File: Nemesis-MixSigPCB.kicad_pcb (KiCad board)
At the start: 4 copper layers, 50 x 60 mm, 113 parts, among them J200 USB_C_Receptacle_USB2.0, J201 2x5 1.27mm, J300 031-5640-1010, J400 031-5640-1010, U100 HT7533-1, U101 TLV62569DBV, U102 MCP6001T-E/OT, U200 STM32F103CBT6, U201 USBLC6-2SC6, U300 MCP6001T-E/OT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

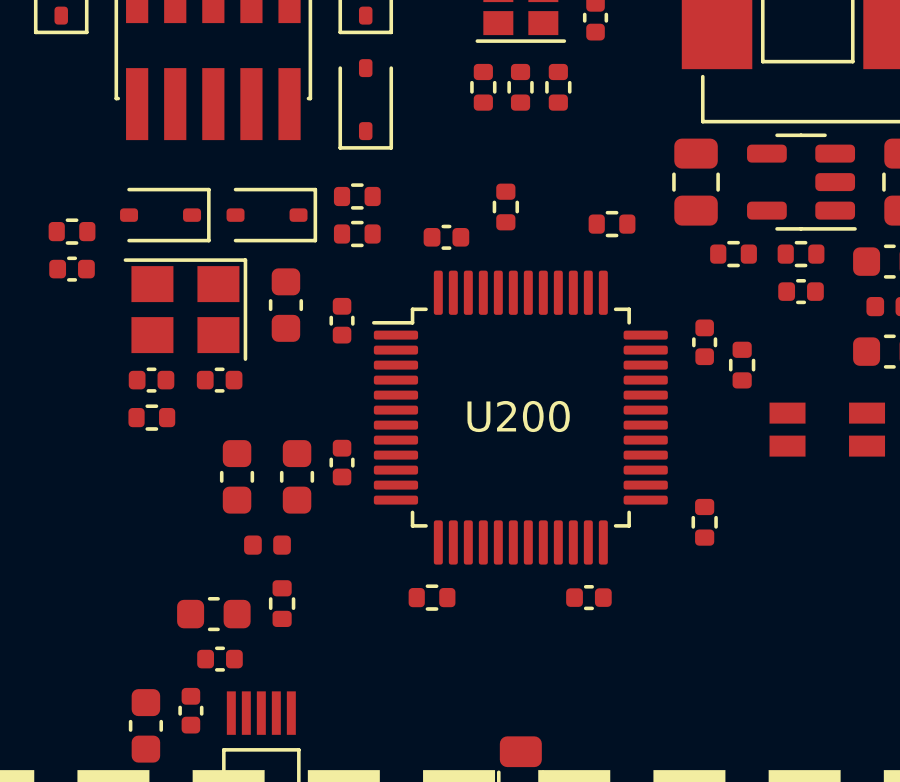
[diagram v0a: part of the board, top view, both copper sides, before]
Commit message: Routed uController Basic Tracks
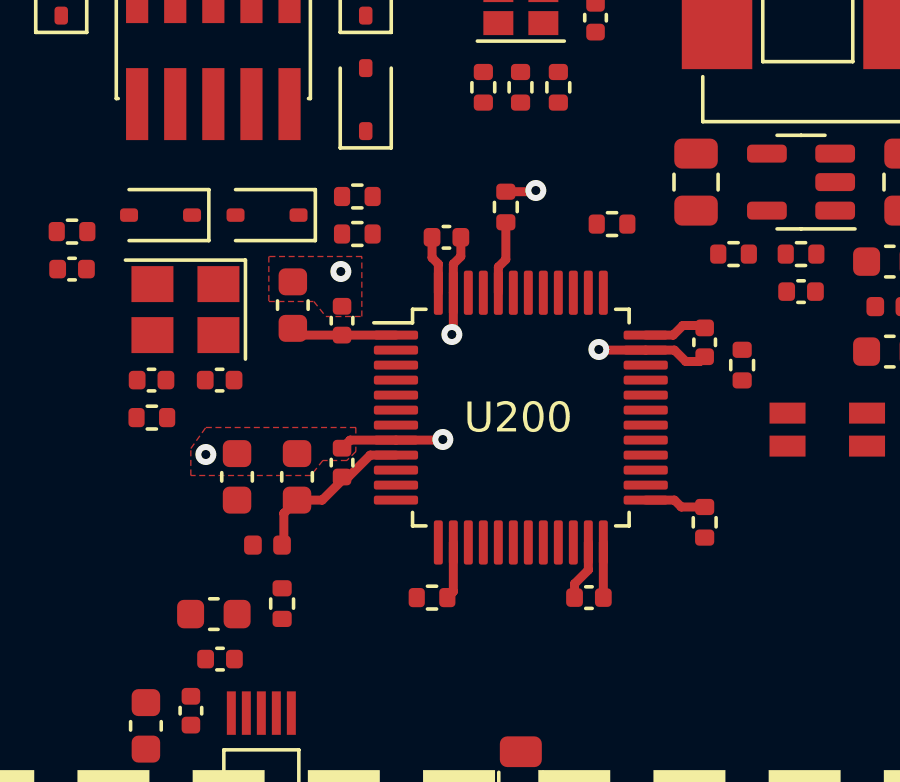
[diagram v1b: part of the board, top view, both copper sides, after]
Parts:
- moved C200 0.23 mm to (137.4, 79.2)
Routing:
- net GND: track 0.00 -> 13.6 mm, vias 0 -> 6
- net +3V3: track 0.00 -> 9.43 mm
- net VDDA: track 0.00 -> 5.69 mm
- net /MCU/BOOT0: track 0.00 -> 2.45 mm
- net SPI2_NSS: track 0.00 -> 2.06 mm
- net SPI1_NSS: track 0.00 -> 1.92 mm
- added copper zone on F.Cu, net GND
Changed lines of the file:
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@@
   )
   (footprint "Capacitor_SMD:C_0603_1608Metric" (layer "F.Cu")
-    (at 137.17 79.22 90)
+    (at 137.4 79.22 90)
     (descr "Capacitor SMD 0603 (1608 Metric), square (rectangular) end terminal, IPC_7351 nominal, (Body size source: IPC-SM-782 page 76, https://www.pcb-3d.com/wordpress/wp-content/uploads/ipc-sm-782a_amendment_1_and_2.pdf), generated with kicad-footprint-generator")
     (tags "capacitor")
@@
     (style (thickness 0.1) (arrow_length 1.27) (text_position_mode 0) (extension_height 0.58642) (extension_offset 0.5) keep_text_aligned)
   )
+  (segment (start 147.25 88.05) (end 146.79 88.51) (width 0.3) (layer "F.Cu") (net 2))
+  (segment (start 140.8375 83.72) (end 142.38 83.72) (width 0.3) (layer "F.Cu") (net 2))
+  (segment (start 149.1625 80.72) (end 150.12 80.72) (width 0.3) (layer "F.Cu") (net 2))
+  (segment (start 143 77.6) (end 143 76.96) (width 0.3) (layer "F.Cu") (net 2))
+  (segment (start 142.38 83.72) (end 142.4 83.7) (width 0.3) (layer "F.Cu") (net 2))
+  (segment (start 142.75 78.8075) (end 142.75 80.15) (width 0.3) (layer "F.Cu") (net 2))
+  (segment (start 145.46 75.44) (end 145.5 75.4) (width 0.3) (layer "F.Cu") (net 2))
+  (segment (start 142.75 78.8075) (end 142.75 77.85) (width 0.3) (layer "F.Cu") (net 2))
+  (segment (start 147.25 87.1325) (end 147.25 88.05) (width 0.3) (layer "F.Cu") (net 2))
+  (segment (start 144.5 75.44) (end 145.46 75.44) (width 0.3) (layer "F.Cu") (net 2))
+  (segment (start 142.75 80.15) (end 142.7 80.2) (width 0.3) (layer "F.Cu") (net 2))
+  (segment (start 146.79 88.51) (end 146.79 88.97) (width 0.3) (layer "F.Cu") (net 2))
+  (segment (start 150.5 81.1) (end 150.9675 81.1) (width 0.3) (layer "F.Cu") (net 2))
+  (segment (start 139.31 83.72) (end 139.04 83.99) (width 0.3) (layer "F.Cu") (net 2))
+  (segment (start 142.75 77.85) (end 143 77.6) (width 0.3) (layer "F.Cu") (net 2))
+  (segment (start 150.12 80.72) (end 150.5 81.1) (width 0.3) (layer "F.Cu") (net 2))
+  (segment (start 147.62 80.72) (end 147.6 80.7) (width 0.3) (layer "F.Cu") (net 2))
+  (segment (start 149.1625 80.72) (end 147.62 80.72) (width 0.3) (layer "F.Cu") (net 2))
+  (segment (start 150.9675 81.1) (end 151.1275 80.94) (width 0.3) (layer "F.Cu") (net 2))
+  (segment (start 140.8375 83.72) (end 139.31 83.72) (width 0.3) (layer "F.Cu") (net 2))
+  (via (at 142.4 83.7) (size 0.7) (drill 0.3) (layers "F.Cu" "B.Cu") (net 2))
+  (via (at 142.7 80.2) (size 0.7) (drill 0.3) (layers "F.Cu" "B.Cu") (net 2))
+  (via (at 147.6 80.7) (size 0.7) (drill 0.3) (layers "F.Cu" "B.Cu") (net 2))
+  (via (at 145.5 75.4) (size 0.7) (drill 0.3) (layers "F.Cu" "B.Cu") (net 2))
+  (via (at 139 78.1) (size 0.7) (drill 0.3) (layers "F.Cu" "B.Cu") (free) (net 2))
+  (via (at 134.5 84.2) (size 0.7) (drill 0.3) (layers "F.Cu" "B.Cu") (free) (net 2))
+  (segment (start 142.25 77.85) (end 142.04 77.64) (width 0.3) (layer "F.Cu") (net 6))
+  (segment (start 142.25 78.8075) (end 142.25 77.85) (width 0.3) (layer "F.Cu") (net 6))
+  (segment (start 140.8375 80.22) (end 139.04 80.22) (width 0.3) (layer "F.Cu") (net 6))
+  (segment (start 149.1625 80.22) (end 150.08 80.22) (width 0.3) (layer "F.Cu") (net 6))
+  (segment (start 150.4 79.9) (end 151.0475 79.9) (width 0.3) (layer "F.Cu") (net 6))
+  (segment (start 150.08 80.22) (end 150.4 79.9) (width 0.3) (layer "F.Cu") (net 6))
+  (segment (start 147.75 87.1325) (end 147.75 88.97) (width 0.3) (layer "F.Cu") (net 6))
+  (segment (start 139.04 80.22) (end 137.625 80.22) (width 0.3) (layer "F.Cu") (net 6))
+  (segment (start 142.04 77.64) (end 142.04 76.96) (width 0.3) (layer "F.Cu") (net 6))
+  (segment (start 151.0475 79.9) (end 151.1275 79.98) (width 0.3) (layer "F.Cu") (net 6))
+  (segment (start 137.625 80.22) (end 137.4 79.995) (width 0.3) (layer "F.Cu") (net 6))
+  (segment (start 137.1 86.16) (end 137.1 87.16) (width 0.3) (layer "F.Cu") (net 9))
+  (segment (start 140.8375 84.22) (end 139.98 84.22) (width 0.3) (layer "F.Cu") (net 9))
+  (segment (start 137.54 85.72) (end 137.1 86.16) (width 0.3) (layer "F.Cu") (net 9))
+  (segment (start 139.04 84.95) (end 139.04 85.06) (width 0.3) (layer "F.Cu") (net 9))
+  (segment (start 139.04 85.06) (end 138.38 85.72) (width 0.3) (layer "F.Cu") (net 9))
+  (segment (start 138.38 85.72) (end 137.54 85.72) (width 0.3) (layer "F.Cu") (net 9))
+  (segment (start 137.1 87.16) (end 137.04 87.22) (width 0.3) (layer "F.Cu") (net 9))
+  (segment (start 139.98 84.22) (end 139.25 84.95) (width 0.3) (layer "F.Cu") (net 9))
+  (segment (start 139.25 84.95) (end 139.04 84.95) (width 0.3) (layer "F.Cu") (net 9))
   (segment (start 138.99 76.9) (end 139.04 76.85) (width 0.3) (layer "F.Cu") (net 34))
+  (segment (start 144.5 77.7) (end 144.5 76.46) (width 0.3) (layer "F.Cu") (net 52))
+  (segment (start 144.25 78.8075) (end 144.25 77.95) (width 0.3) (layer "F.Cu") (net 52))
+  (segment (start 144.25 77.95) (end 144.5 77.7) (width 0.3) (layer "F.Cu") (net 52))
+  (segment (start 150.35 85.95) (end 151.1275 85.95) (width 0.3) (layer "F.Cu") (net 54))
+  (segment (start 150.12 85.72) (end 150.35 85.95) (width 0.3) (layer "F.Cu") (net 54))
+  (segment (start 149.1625 85.72) (end 150.12 85.72) (width 0.3) (layer "F.Cu") (net 54))
+  (segment (start 142.75 87.1325) (end 142.75 88.77) (width 0.3) (layer "F.Cu") (net 55))
+  (segment (start 142.75 88.77) (end 142.55 88.97) (width 0.3) (layer "F.Cu") (net 55))
   (segment (start 143.75 72.51) (end 143.79 72.47) (width 0.3) (layer "F.Cu") (net 56))
+  (zone (net 2) (net_name "GND") (layer "F.Cu") (hatch edge 0.5)
+    (priority 1)
+    (connect_pads (clearance 0.2))
+    (min_thickness 0.25) (filled_areas_thickness no)
+    (fill yes (thermal_gap 0.5) (thermal_bridge_width 0.5))
+    (polygon
+      (pts
+        (xy 136.6 79.1)
+        (xy 138.1 79.1)
+        (xy 138.5 79.6)
+        (xy 139.7 79.6)
+        (xy 139.7 77.6)
+        (xy 136.6 77.6)
+      )
+    )
+  )
+  (zone (net 2) (net_name "GND") (layer "F.Cu") (hatch edge 0.5)
+    (priority 2)
+    (connect_pads (clearance 0.2))
+    (min_thickness 0.25) (filled_areas_thickness no)
+    (fill yes (thermal_gap 0.5) (thermal_bridge_width 0.5))
+    (polygon
+      (pts
+        (xy 139.5 84.1)
+        (xy 139.2 84.4)
+        (xy 138.4 84.4)
+        (xy 138 84.9)
+        (xy 134 84.9)
+        (xy 134 84)
+        (xy 134.5 83.3)
+        (xy 139.5 83.3)
+      )
+    )
+  )
   (zone (net 2) (net_name "GND") (layers "In1.Cu" "In2.Cu") (hatch edge 0.5)
     (connect_pads (clearance 0.4))

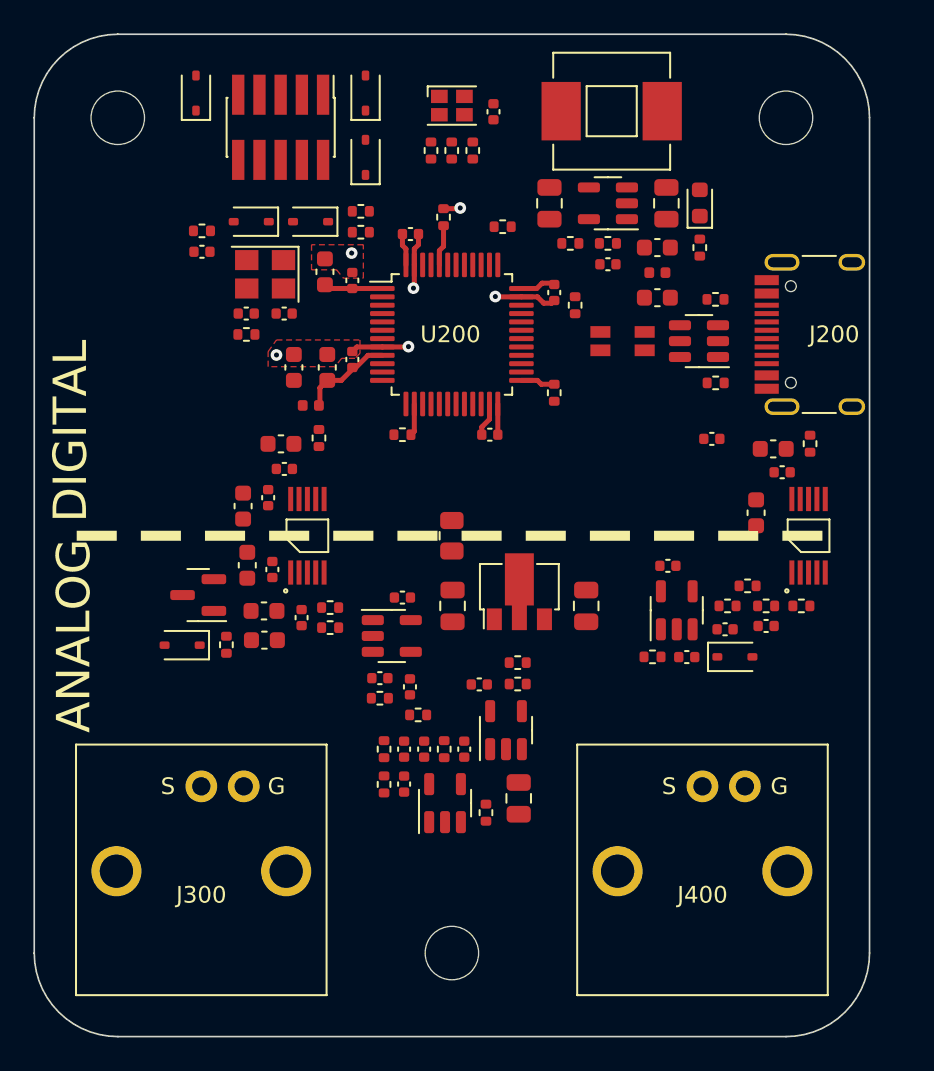
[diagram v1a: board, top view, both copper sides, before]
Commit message: Initial Ground Pours done
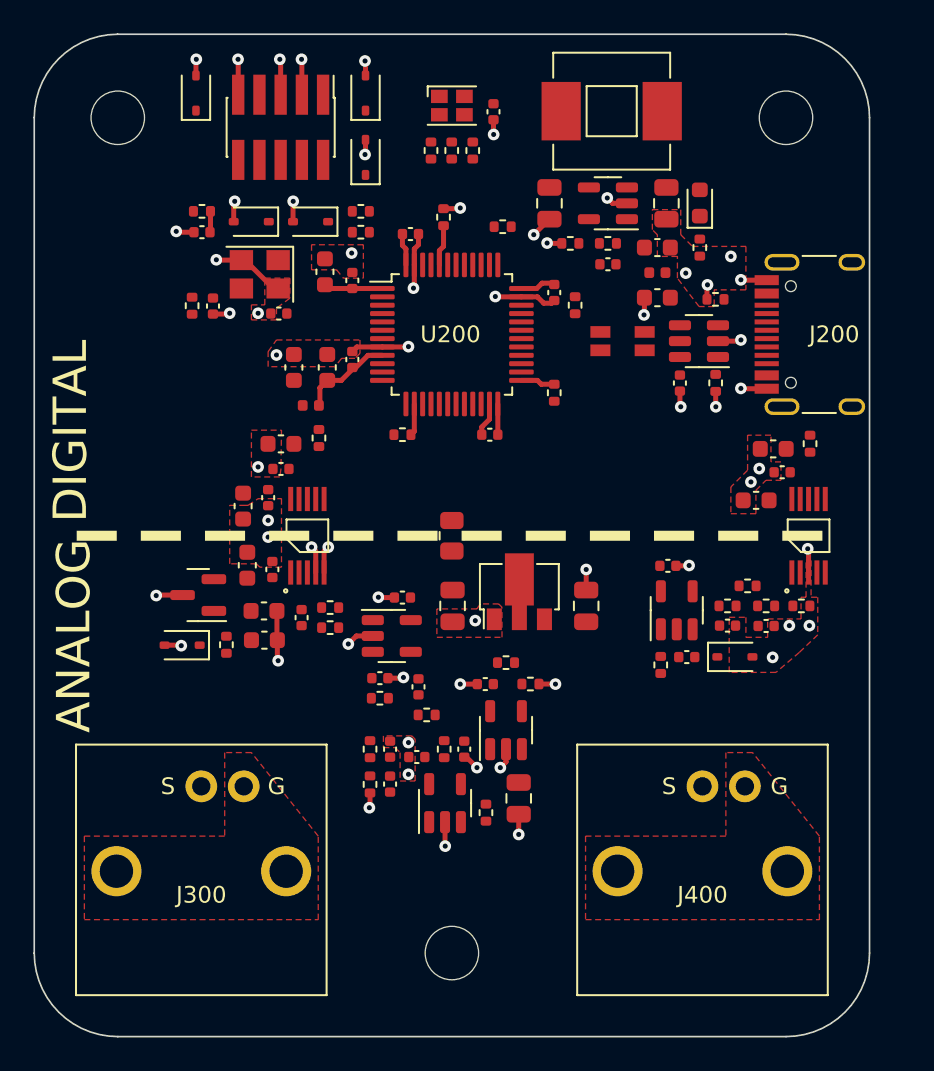
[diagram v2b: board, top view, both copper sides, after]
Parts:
- moved C210 3.85 mm to (158.7, 85.9), turned to -90 degrees
- moved R201 3.68 mm to (129.4, 81.2), turned to 90 degrees
- moved C209 2.04 mm to (130.7, 81.3), turned to -90 degrees
- moved C212 1.17 mm to (130.0, 76.8)
- moved R213 1.17 mm to (130.0, 75.6)
- moved R300 0.84 mm to (140.1, 107.8)
- moved R301 0.84 mm to (140.1, 109.9)
- moved C300 0.84 mm to (141.3, 107.8)
- moved C301 0.84 mm to (141.3, 109.9)
- moved R105 0.76 mm to (149.7, 103.9), turned to 180 degrees
- moved C402 0.74 mm to (163.2, 92.9), turned to 180 degrees
- moved R104 0.70 mm to (148.2, 102.6)
- moved R405 0.69 mm to (157.5, 102.8), turned to 90 degrees
- moved C302 0.64 mm to (142.9, 108.3), turned to 180 degrees
- moved R304 0.51 mm to (143.5, 105.7)
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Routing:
- net GND: track 13.6 -> 69.1 mm, vias 6 -> 60
- net /MCU/NRST: track 0.00 -> 1.26 mm

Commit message: Ignored KiCAD Backups Folder
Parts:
- moved R206 8.19 mm to (168.0, 77.0), turned to 0 degrees
- moved R205 7.76 mm to (167.9, 89.0), turned to 0 degrees
- moved R307 1.59 mm to (137.6, 100.9), turned to -90 degrees
- moved R309 1.51 mm to (136.3, 90.5)
- moved R203 1.42 mm to (141.0, 88.0), turned to -90 degrees
- moved R306 1.37 mm to (136.4, 100.9), turned to -90 degrees
- moved C307 1.23 mm to (137.0, 99.2), turned to 0 degrees
- moved R400 1.19 mm to (166.4, 90.7)
- moved C314 1.19 mm to (133.6, 90.9)
- moved C315 1.19 mm to (133.6, 89.4)
- moved C208 0.84 mm to (135.5, 81.7)
- moved C210 0.23 mm to (158.5, 85.7), turned to 180 degrees
- moved R200 0.12 mm to (144.6, 75.9)
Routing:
- net /MCU/NRST: track 1.26 -> 20.3 mm
- net VBUS: track 0.00 -> 18.6 mm
- net SPI1_MISO: track 0.00 -> 13.5 mm
- net /MCU/HSE_OUT: track 0.00 -> 11.8 mm
- net /MCU/HSE_IN: track 0.00 -> 10.3 mm
- net /MCU/CONN_NRST: track 0.00 -> 10.1 mm
- net SPI1_SCK: track 0.00 -> 9.29 mm
- net SPI1_NSS: track 1.92 -> 9.61 mm, vias 0 -> 2
- net /MCU/TIM4_CH2: track 0.00 -> 6.94 mm
- net /MCU/USB_CONN_D-: track 0.00 -> 6.93 mm
- net /MCU/USB_CONN_CC1: track 0.00 -> 6.87 mm
- net /MCU/TIM4_CH1: track 0.00 -> 6.75 mm
- net /MCU/USB_CONN_CC2: track 0.00 -> 6.55 mm
- net /MCU/TIM4_CH3: track 0.06 -> 6.39 mm
- net /MCU/USB_CONN_D+: track 0.00 -> 6.09 mm
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
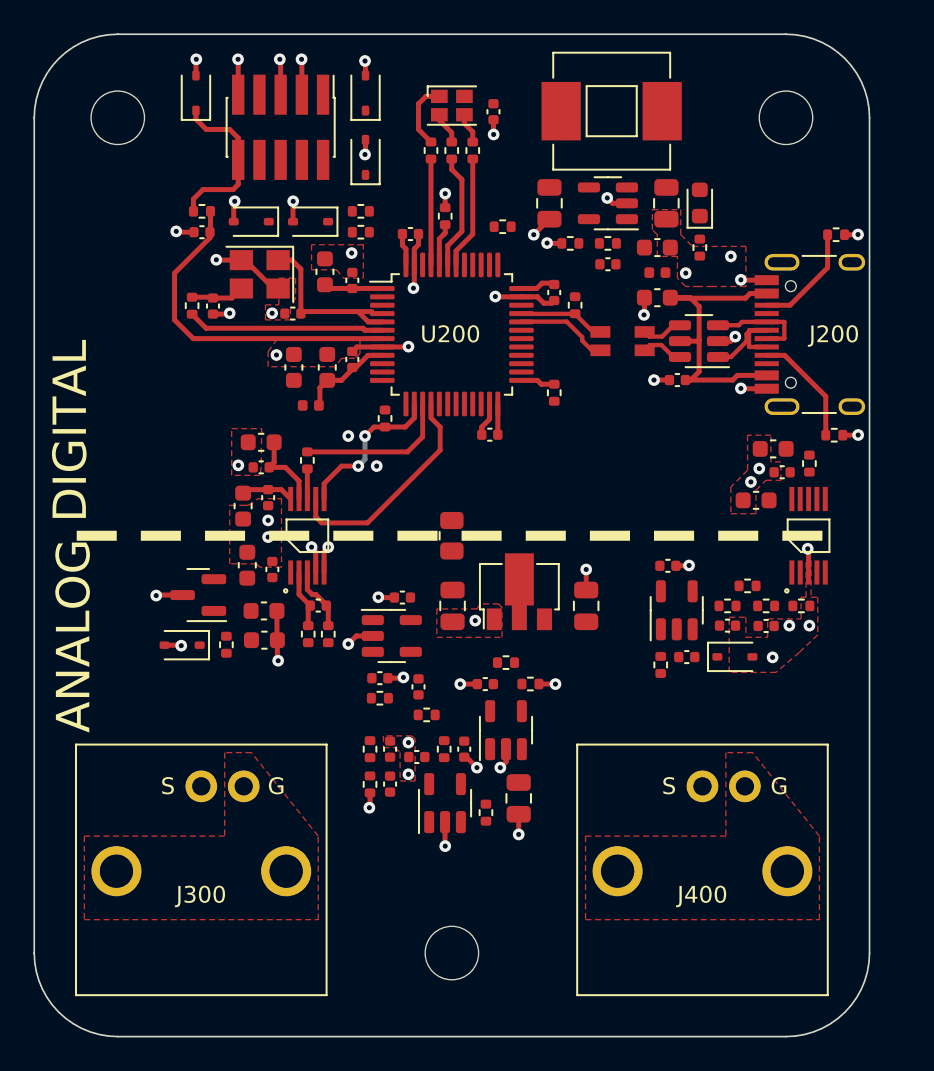
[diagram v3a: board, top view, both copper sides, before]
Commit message: Routed Digital Side of Board
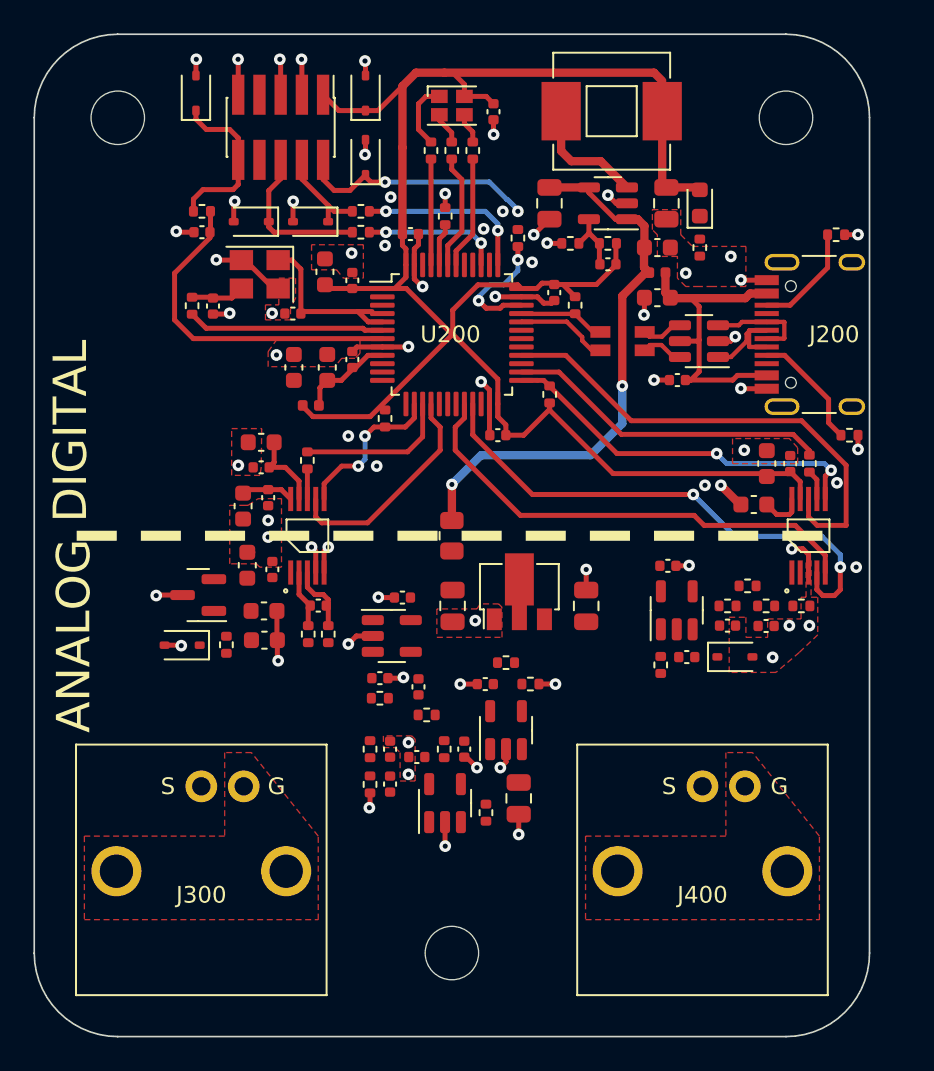
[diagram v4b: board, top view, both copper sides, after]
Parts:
- moved R210 1.14 mm to (148.9, 77.2), turned to 90 degrees
- moved C400 0.96 mm to (163.8, 90.7), turned to 90 degrees
- moved R205 0.91 mm to (168.8, 89.0)
- moved C401 0.71 mm to (165.2, 90.7), turned to 90 degrees
- moved C202 0.48 mm to (147.8, 89.0)
- moved R202 0.29 mm to (150.8, 86.6)
- moved C402 0.28 mm to (163.1, 93.2)
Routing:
- net +3V3: track 14.3 -> 118.8 mm
- net +5V: track 0.00 -> 33.5 mm, vias 0 -> 2
- net DAC_NLDAC: track 0.00 -> 31.6 mm, vias 0 -> 2
- net SPI2_MOSI: track 0.00 -> 29.3 mm
- net DAC_NCLR: track 0.00 -> 28.8 mm
- net SPI2_NSS: track 2.06 -> 22.6 mm, vias 0 -> 2
- net SPI2_SCK: track 0.00 -> 19.5 mm
- net /MCU/CONN_SWDIO: track 0.00 -> 14.5 mm, vias 0 -> 2
- net /MCU/SWCLK: track 0.00 -> 10.5 mm, vias 0 -> 2
- net /MCU/CONN_SWO: track 0.07 -> 9.51 mm
- net /MCU/SWO: track 0.00 -> 8.27 mm, vias 0 -> 2
- net /MCU/SWDIO: track 0.00 -> 7.50 mm, vias 0 -> 2
- net /Power/BUCK_SW: track 0.00 -> 7.23 mm
- net /MCU/CONN_SWCLK: track 0.00 -> 5.94 mm
- net GND: track 69.0 -> 72.9 mm, vias 62 -> 71
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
